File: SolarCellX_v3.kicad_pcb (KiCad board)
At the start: 6 copper layers, 48.4 x 48.4 mm, 55 parts, among them J1 XF2M-1015-1A, U2 Value, U3 TSL2561

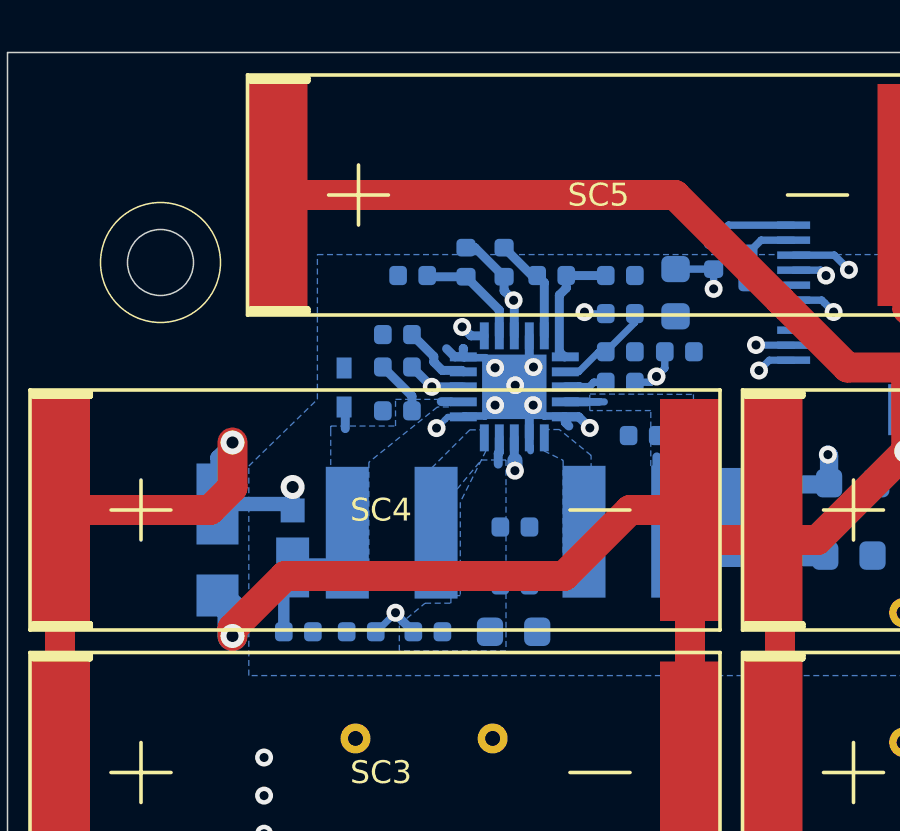
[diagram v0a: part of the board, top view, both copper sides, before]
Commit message: moved diode to fix mechanical collision
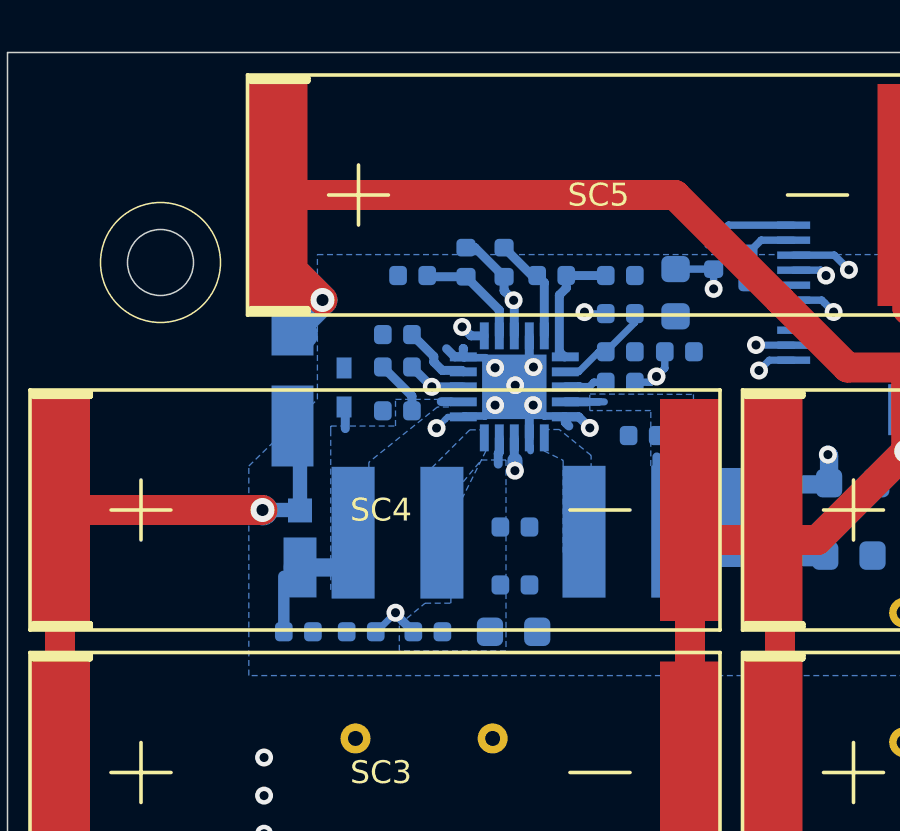
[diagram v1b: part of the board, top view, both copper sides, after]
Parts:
- moved D4 5.59 mm to (99.5, 51.2), turned to 90 degrees
- moved D3 0.25 mm to (99.8, 56.5)
- moved L1 0.19 mm to (103.0, 56.0)
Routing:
- net Net-(D4-Pad2): track 106.4 -> 93.7 mm
- net /VSOLAR_FULL: track 56.7 -> 54.1 mm, vias 2 -> 1
